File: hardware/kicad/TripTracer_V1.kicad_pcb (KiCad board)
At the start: 2 copper layers, 21 parts, among them J201 J1_GCT_USB4105_GF_A_USB_C, U101 U3_TI_LMR36510ADDAR_DDA, U201 U1_ESP32-S3-MINI-1-N8

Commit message: Synchronize existing PCB nets and test idealized HOLD transitions
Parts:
- C101: value C_1210_3225 -> 4.7uF 100V X7R VIN
- C102: value C_1206_3216 -> 100nF BOOT-SW
- C103: value C_1206_3216 -> 1uF VCC
- C104, C105: value C_1210_3225 -> 22uF 25V X7R VOUT
- C201: value C_1210_3225 -> 100nF MCU local
- C202: value C_1210_3225 -> 22uF MCU bulk
- C203: value C_1210_3225 -> 1uF EN RC
- D201: value D2_ST_USBLC6_2SC6 -> USBLC6-2SC6
- J201: value J1_GCT_USB4105_GF_A_USB_C -> GCT USB4105-GF-A
- R101: value R_1206_3216 -> 100k 1% FB TOP TI
- R102: value R_1206_3216 -> 24.9k 1% FB BOTTOM TI
- R201: value R_1206_3216 -> 5.1k CC1
- R202: value R_1206_3216 -> 5.1k CC2
- R203: value R_1206_3216 -> 22R D+
- R204: value R_1206_3216 -> 22R D-
- R205: value R_1206_3216 -> 10k BOOT PU
- R206: value R_1206_3216 -> 10k EN PU
- U101: value U3_TI_LMR36510ADDAR_DDA -> LMR36520ADDAR 5V/2A CANDIDATE
- U201: value U1_ESP32-S3-MINI-1-N8 -> ESP32-S3-MINI-1-N8
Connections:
- C101 pad 1: (no net) -> GND
- C101 pad 2: (no net) -> HV_PROTECTED_AFTER_EFUSE
- C102 pad 1: (no net) -> Net-(U101-BOOT)
- C102 pad 2: (no net) -> Net-(U101-SW)
- C103 pad 1: (no net) -> Net-(U101-VCC)
- C103 pad 2: (no net) -> GND
- C104 pad 1: (no net) -> GND
- C104 pad 2: (no net) -> V5_BUCK_RAW
- C105 pad 1: (no net) -> GND
- C105 pad 2: (no net) -> V5_BUCK_RAW
- C201 pad 1: (no net) -> GND
- C201 pad 2: (no net) -> V3V3_SYS
- C202 pad 1: (no net) -> GND
- C202 pad 2: (no net) -> V3V3_SYS
- C203 pad 1: (no net) -> GND
- C203 pad 2: (no net) -> EN_RESET
- D201 pad 1: (no net) -> USB_DP_PORT
- D201 pad 2: (no net) -> GND
- D201 pad 3: (no net) -> USB_DM_PORT
- D201 pad 4: (no net) -> USB_DM_PORT_ESD
- D201 pad 5: (no net) -> USB_VBUS_RAW
- D201 pad 6: (no net) -> Net-(D201-IO1_OUT)
- J201 pad A1: (no net) -> GND
- J201 pad A12: (no net) -> GND
- J201 pad A4: (no net) -> USB_VBUS_RAW
- J201 pad A5: (no net) -> Net-(J201-CC1)
- J201 pad A6: (no net) -> USB_DP_PORT
- J201 pad A7: (no net) -> USB_DM_PORT
- J201 pad A8: (no net) -> unconnected-(J201-SBU1-PadA8)
- J201 pad A9: (no net) -> USB_VBUS_RAW
- J201 pad B1: (no net) -> GND
- J201 pad B12: (no net) -> GND
- J201 pad B4: (no net) -> USB_VBUS_RAW
- J201 pad B5: (no net) -> Net-(J201-CC2)
- J201 pad B6: (no net) -> USB_DP_PORT
- J201 pad B7: (no net) -> USB_DM_PORT
- J201 pad B8: (no net) -> unconnected-(J201-SBU2-PadB8)
- J201 pad B9: (no net) -> USB_VBUS_RAW
- J201 pad SH: (no net) -> GND
- L101 pad 1: (no net) -> Net-(U101-SW)
- L101 pad 2: (no net) -> V5_BUCK_RAW
- R101 pad 1: (no net) -> Net-(U101-FB)
- R101 pad 2: (no net) -> V5_BUCK_RAW
- R102 pad 1: (no net) -> GND
- R102 pad 2: (no net) -> Net-(U101-FB)
- R201 pad 1: (no net) -> GND
- R201 pad 2: (no net) -> Net-(J201-CC1)
- R202 pad 1: (no net) -> Net-(J201-CC2)
- R202 pad 2: (no net) -> GND
- R203 pad 1: (no net) -> Net-(D201-IO1_OUT)
- R203 pad 2: (no net) -> USB_DP_MCU
- R204 pad 1: (no net) -> USB_DM_PORT_ESD
- R204 pad 2: (no net) -> USB_DM_MCU
- R205 pad 1: (no net) -> BOOT0_RECOVERY
- R205 pad 2: (no net) -> V3V3_SYS
- R206 pad 1: (no net) -> EN_RESET
- R206 pad 2: (no net) -> V3V3_SYS
- U101 pad 1: (no net) -> GND
- U101 pad 2: (no net) -> HV_PROTECTED_AFTER_EFUSE
- U101 pad 3: (no net) -> BUCK_ENABLE
- U101 pad 4: (no net) -> /5-V-Synchronbuck (elektrischer Entwurf)/BUCK_PGOOD
- U101 pad 5: (no net) -> Net-(U101-FB)
- U101 pad 6: (no net) -> Net-(U101-VCC)
- U101 pad 7: (no net) -> Net-(U101-BOOT)
- U101 pad 8: (no net) -> Net-(U101-SW)
- U101 pad 9: (no net) -> GND
- U201 pad 1: (no net) -> GND
- U201 pad 10: (no net) -> unconnected-(U201-IO6-Pad10)
- U201 pad 11: (no net) -> unconnected-(U201-IO7-Pad11)
- U201 pad 12: (no net) -> unconnected-(U201-IO8-Pad12)
- U201 pad 13: (no net) -> unconnected-(U201-IO9-Pad13)
- U201 pad 14: (no net) -> unconnected-(U201-IO10-Pad14)
- U201 pad 15: (no net) -> unconnected-(U201-IO11-Pad15)
- U201 pad 16: (no net) -> unconnected-(U201-IO12-Pad16)
- U201 pad 17: (no net) -> unconnected-(U201-IO13-Pad17)
- U201 pad 18: (no net) -> unconnected-(U201-IO14-Pad18)
- U201 pad 19: (no net) -> unconnected-(U201-IO15-Pad19)
- U201 pad 2: (no net) -> GND
- U201 pad 20: (no net) -> unconnected-(U201-IO16-Pad20)
- U201 pad 21: (no net) -> unconnected-(U201-IO17-Pad21)
- U201 pad 22: (no net) -> unconnected-(U201-IO18-Pad22)
- U201 pad 23: (no net) -> USB_DM_MCU
- U201 pad 24: (no net) -> USB_DP_MCU
- U201 pad 25: (no net) -> unconnected-(U201-IO21-Pad25)
- U201 pad 26: (no net) -> unconnected-(U201-IO26-Pad26)
- U201 pad 27: (no net) -> unconnected-(U201-IO47-Pad27)
- U201 pad 28: (no net) -> unconnected-(U201-IO33-Pad28)
- U201 pad 29: (no net) -> unconnected-(U201-IO34-Pad29)
- U201 pad 3: (no net) -> V3V3_SYS
- U201 pad 30: (no net) -> unconnected-(U201-IO48-Pad30)
- U201 pad 31: (no net) -> unconnected-(U201-IO35-Pad31)
- U201 pad 32: (no net) -> unconnected-(U201-IO36-Pad32)
- U201 pad 33: (no net) -> unconnected-(U201-IO37-Pad33)
- U201 pad 34: (no net) -> unconnected-(U201-IO38-Pad34)
- U201 pad 35: (no net) -> unconnected-(U201-IO39-Pad35)
- U201 pad 36: (no net) -> unconnected-(U201-IO40-Pad36)
- U201 pad 37: (no net) -> unconnected-(U201-IO41-Pad37)
- U201 pad 38: (no net) -> unconnected-(U201-IO42-Pad38)
- U201 pad 39: (no net) -> unconnected-(U201-TXD0_IO43-Pad39)
- U201 pad 4: (no net) -> BOOT0_RECOVERY
- U201 pad 40: (no net) -> unconnected-(U201-RXD0_IO44-Pad40)
- U201 pad 41: (no net) -> unconnected-(U201-IO45-Pad41)
- U201 pad 42: (no net) -> GND
- U201 pad 43: (no net) -> GND
- U201 pad 44: (no net) -> unconnected-(U201-IO46-Pad44)
- U201 pad 45: (no net) -> EN_RESET
- U201 pad 46: (no net) -> GND
- U201 pad 47: (no net) -> GND
- U201 pad 48: (no net) -> GND
- U201 pad 49: (no net) -> GND
- U201 pad 5: (no net) -> unconnected-(U201-IO1-Pad5)
- U201 pad 50: (no net) -> GND
- U201 pad 51: (no net) -> GND
- U201 pad 52: (no net) -> GND
- U201 pad 53: (no net) -> GND
- U201 pad 54: (no net) -> GND
- U201 pad 55: (no net) -> GND
- U201 pad 56: (no net) -> GND
- U201 pad 57: (no net) -> GND
- U201 pad 58: (no net) -> GND
- U201 pad 59: (no net) -> GND
- U201 pad 6: (no net) -> unconnected-(U201-IO2-Pad6)
- U201 pad 60: (no net) -> GND
- U201 pad 61: (no net) -> GND
- U201 pad 62: (no net) -> GND
- U201 pad 63: (no net) -> GND
- U201 pad 64: (no net) -> GND
- U201 pad 65: (no net) -> GND
- U201 pad 7: (no net) -> unconnected-(U201-IO3-Pad7)
- U201 pad 8: (no net) -> unconnected-(U201-IO4-Pad8)
- U201 pad 9: (no net) -> unconnected-(U201-IO5-Pad9)

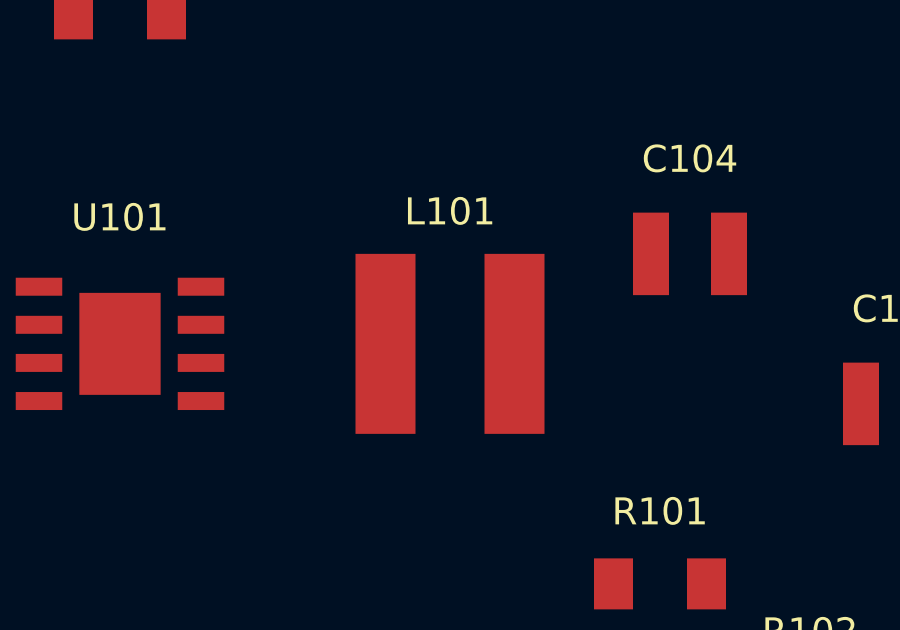
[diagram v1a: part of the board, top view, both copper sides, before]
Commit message: Match PCB inductor to Bourns geometry and qualify current assumptions
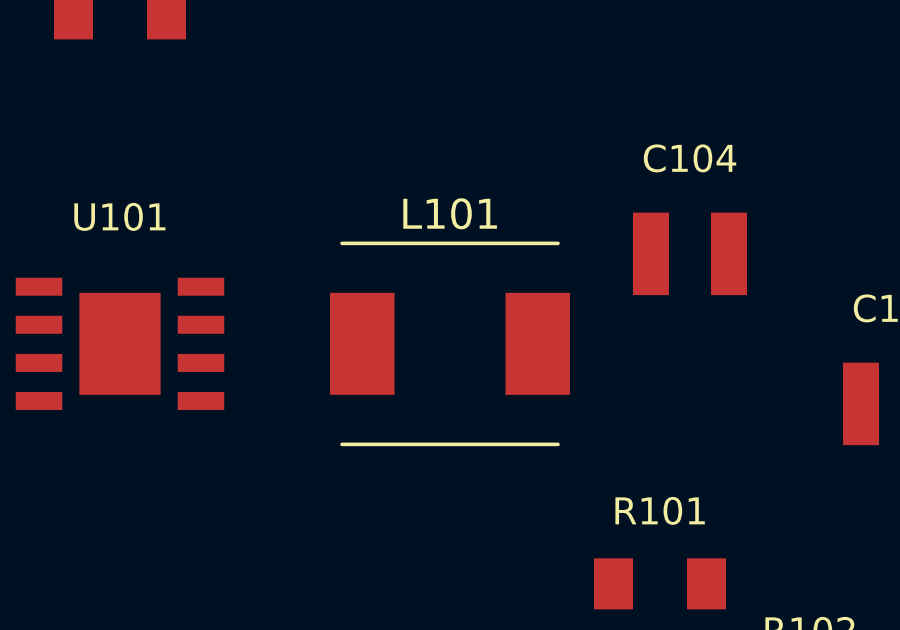
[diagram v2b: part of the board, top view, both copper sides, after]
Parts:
- L101: value L1_Bourns_SRN6045_220M -> 10uH Bourns SRP6030VA-100M (Isat typ 5A); footprint Tripmaster:L1_Bourns_SRN6045_220M -> Tripmaster:L_Bourns_SRP6030VA_100M
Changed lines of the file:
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@@
 		)
 	)
-	(footprint "Tripmaster:L1_Bourns_SRN6045_220M"
+	(footprint "Tripmaster:L_Bourns_SRP6030VA_100M"
 		(layer "F.Cu")
 		(at 74 52)
-		(descr "Bourns SRN6045-100M 22uH; current rating verify, layout: two 2x6mm pads, gap 2.3mm | Status: HERSTELLER_LANDMASS_ELEKTRIK_PRUEFEN")
-		(tags "Tripmaster")
+		(descr "Bourns SRP6030VA-100M 10uH Irms/Isat typ 5A AEC-Q200; land-pattern per Bourns PDF 8.0mm outside, 3.7mm gap, 3.4mm height. Preliminary footprint, 3D model not included.")
+		(tags "SRP6030VA 10uH 5A")
 		(property "Reference" "L101"
-			(at 0 -4.4 0)
+			(at 0 -4.3 0)
 			(layer "F.SilkS")
 			(effects
 				(font
-					(size 0.9 0.9)
-					(thickness 0.13)
+					(size 1 1)
+					(thickness 0.15)
 				)
 			)
 		)
-		(property "Value" "L1_Bourns_SRN6045_220M"
-			(at 0 4.4 0)
+		(property "Value" "10uH Bourns SRP6030VA-100M (Isat typ 5A)"
+			(at 0 4.3 0)
 			(layer "F.Fab")
 			(effects
 				(font
-					(size 0.7 0.7)
-					(thickness 0.1)
+					(size 1 1)
+					(thickness 0.15)
 				)
 			)
@@
 		(attr smd)
 		(duplicate_pad_numbers_are_jumpers no)
+		(fp_line
+			(start -3.6 -3.35)
+			(end 3.6 -3.35)
+			(stroke
+				(width 0.12)
+				(type default)
+			)
+			(layer "F.SilkS")
+		)
+		(fp_line
+			(start -3.6 3.35)
+			(end 3.6 3.35)
+			(stroke
+				(width 0.12)
+				(type default)
+			)
+			(layer "F.SilkS")
+		)
 		(fp_rect
-			(start -3.55 -3.55)
-			(end 3.55 3.55)
+			(start -4.25 -3.8)
+			(end 4.25 3.8)
 			(stroke
 				(width 0.05)
@@
 		)
 		(fp_rect
-			(start -3 -3)
-			(end 3 3)
+			(start -3.55 -3.3)
+			(end 3.55 3.3)
 			(stroke
 				(width 0.1)
@@
 			(layer "F.Fab")
 		)
+		(fp_text user "${REFERENCE}"
+			(at 0 0 0)
+			(layer "F.Fab")
+			(effects
+				(font
+					(size 1 1)
+					(thickness 0.15)
+				)
+			)
+		)
 		(pad "1" smd rect
-			(at -2.15 0)
-			(size 2 6)
+			(at -2.925 0)
+			(size 2.15 3.4)
 			(layers "F.Cu" "F.Mask" "F.Paste")
 			(net "Net-(U101-SW)")
 		)
 		(pad "2" smd rect
-			(at 2.15 0)
-			(size 2 6)
+			(at 2.925 0)
+			(size 2.15 3.4)
 			(layers "F.Cu" "F.Mask" "F.Paste")
 			(net "V5_BUCK_RAW")
 		)
 		(embedded_fonts no)
-		(model "${KIPRJMOD}/Tripmaster_3dmodels.3dshapes/Bourns_SRN6045_100M.step"
-			(offset
-				(xyz 0 0 0)
-			)
-			(scale
-				(xyz 1 1 1)
-			)
-			(rotate
-				(xyz 0 0 0)
-			)
-		)
 	)
 	(footprint "Tripmaster:C_1210_3225"
